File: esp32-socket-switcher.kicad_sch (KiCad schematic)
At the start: 27 parts, among them J1 USB4110GFA, J2 4DB-P108-06, K1 G5CA-1A DC5, Q3 CSD17575Q3T, SW1 SW_SPST

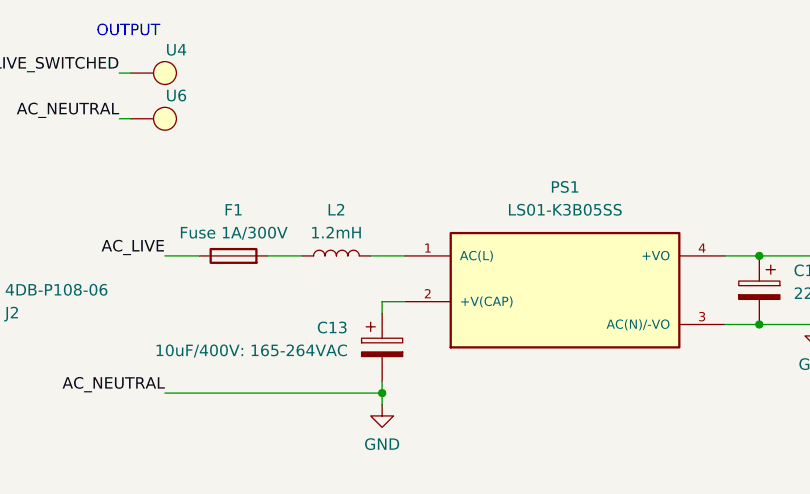
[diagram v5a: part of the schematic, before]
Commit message: added fuse. I feel i have been deceived...
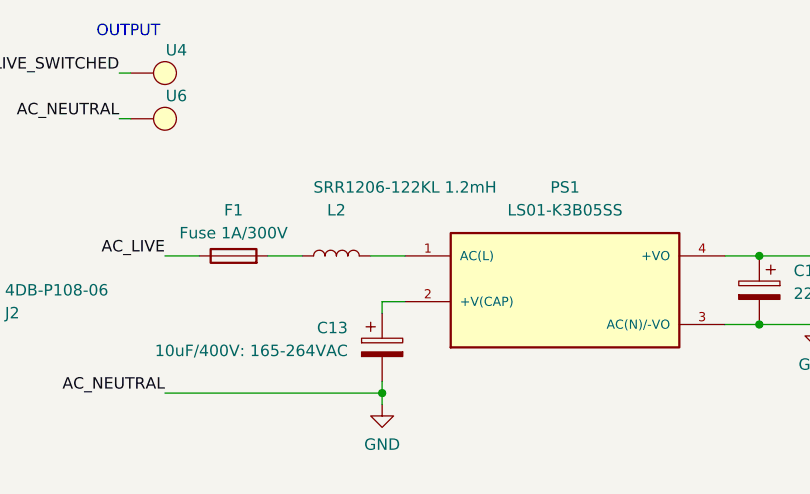
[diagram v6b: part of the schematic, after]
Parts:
- F1: footprint (none) -> esp32-socket-switcher:FUSE_3519; MPN Fuse (none) -> 2JS 1.25-R; MPN Holder (none) -> 3519 (Keystone)
- L2: value 1.2mH -> SRR1206-122KL 1.2mH; footprint (none) -> esp32-socket-switcher:IND_BOURNS_SRR1240
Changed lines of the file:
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@@
       (effects (font (size 1.27 1.27)))
     )
-    (property "Footprint" "" (at 76.2 41.148 90)
+    (property "Footprint" "esp32-socket-switcher:FUSE_3519" (at 76.2 41.148 90)
       (effects (font (size 1.27 1.27)) hide)
     )
     (property "Datasheet" "~" (at 76.2 39.37 0)
+      (effects (font (size 1.27 1.27)) hide)
+    )
+    (property "MPN Fuse" "2JS 1.25-R" (at 76.2 39.37 90)
+      (effects (font (size 1.27 1.27)) hide)
+    )
+    (property "MPN Holder" "3519 (Keystone)" (at 76.2 39.37 90)
       (effects (font (size 1.27 1.27)) hide)
     )
@@
   )
   (symbol (lib_id "esp32-socket-switcher:L") (at 87.63 39.37 90) (unit 1)
-    (in_bom yes) (on_board yes) (dnp no) (fields_autoplaced)
+    (in_bom yes) (on_board yes) (dnp no)
     (property "Reference" "L2" (at 87.63 34.29 90)
       (effects (font (size 1.27 1.27)))
     )
-    (property "Value" "1.2mH" (at 87.63 36.83 90)
-      (effects (font (size 1.27 1.27)))
-    )
-    (property "Footprint" "" (at 87.63 39.37 0)
-      (effects (font (size 1.27 1.27)) hide)
-    )
+    (property "Value" "SRR1206-122KL 1.2mH" (at 95.25 31.75 90)
+      (effects (font (size 1.27 1.27)))
+    )
+    (property "Footprint" "esp32-socket-switcher:IND_BOURNS_SRR1240" (at 87.63 39.37 0)
+      (effects (font (size 1.27 1.27)) hide)
+    )

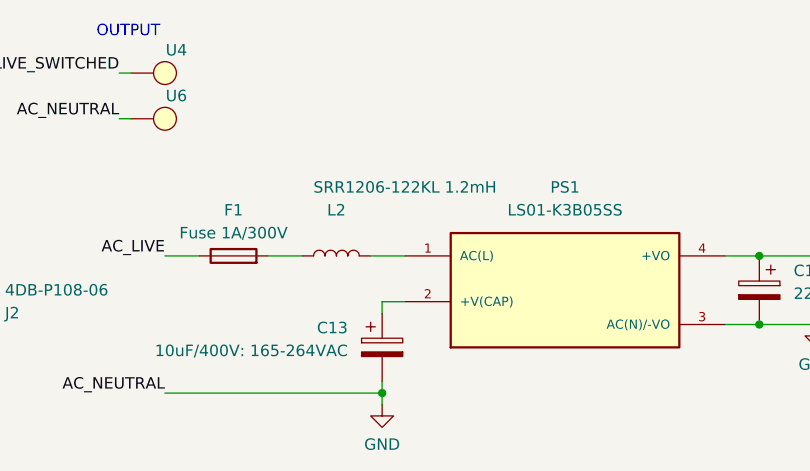
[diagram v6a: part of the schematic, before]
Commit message: changed inductors, sticking with og converter
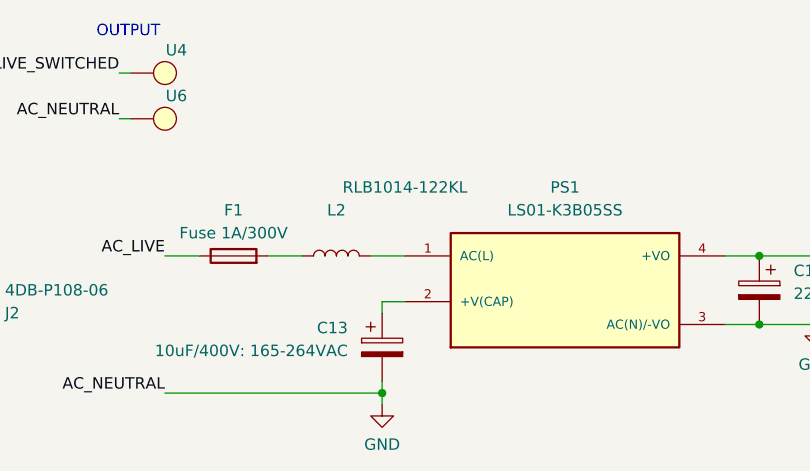
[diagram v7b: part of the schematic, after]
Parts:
- L2: value SRR1206-122KL 1.2mH -> RLB1014-122KL; footprint esp32-socket-switcher:IND_BOURNS_SRR1240 -> esp32-socket-switcher:IND_BOURNS_RLB1014
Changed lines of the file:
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@@
       (effects (font (size 1.27 1.27)))
     )
-    (property "Value" "SRR1206-122KL 1.2mH" (at 95.25 31.75 90)
+    (property "Value" "RLB1014-122KL" (at 95.25 31.75 90)
       (effects (font (size 1.27 1.27)))
     )
-    (property "Footprint" "esp32-socket-switcher:IND_BOURNS_SRR1240" (at 87.63 39.37 0)
+    (property "Footprint" "esp32-socket-switcher:IND_BOURNS_RLB1014" (at 87.63 39.37 0)
       (effects (font (size 1.27 1.27)) hide)
     )

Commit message: routing
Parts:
- C12: value 220uF/16V -> EEE-FK1C221XP; Rating (none) -> 220uF/16V
- C13: value 10uF/400V: 165-264VAC -> UCY2G100MPD; Rating (none) -> 10uF/400V: 165-264VAC
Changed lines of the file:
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@@
       (effects (font (size 1.27 1.27)) (justify right))
     )
-    (property "Value" "10uF/400V: 165-264VAC" (at 88.9 49.911 0)
+    (property "Value" "UCY2G100MPD" (at 88.9 49.911 0)
       (effects (font (size 1.27 1.27)) (justify right))
     )
@@
     )
     (property "Datasheet" "~" (at 92.71 49.53 0)
+      (effects (font (size 1.27 1.27)) hide)
+    )
+    (property "Rating" "10uF/400V: 165-264VAC" (at 92.71 49.53 0)
       (effects (font (size 1.27 1.27)) hide)
     )
@@
       (effects (font (size 1.27 1.27)) (justify right))
     )
-    (property "Value" "220uF/16V" (at 138.43 43.561 0)
+    (property "Value" "EEE-FK1C221XP" (at 138.43 43.561 0)
       (effects (font (size 1.27 1.27)) (justify right))
     )
@@
       (effects (font (size 1.27 1.27)) hide)
     )
+    (property "Rating" "220uF/16V" (at 134.62 43.18 0)
+      (effects (font (size 1.27 1.27)) hide)
+    )
